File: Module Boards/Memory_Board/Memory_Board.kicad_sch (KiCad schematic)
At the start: 12 parts, among them U1 MX25U12832FZNI02-TR, U2 MX25U25643GZ4I00-T

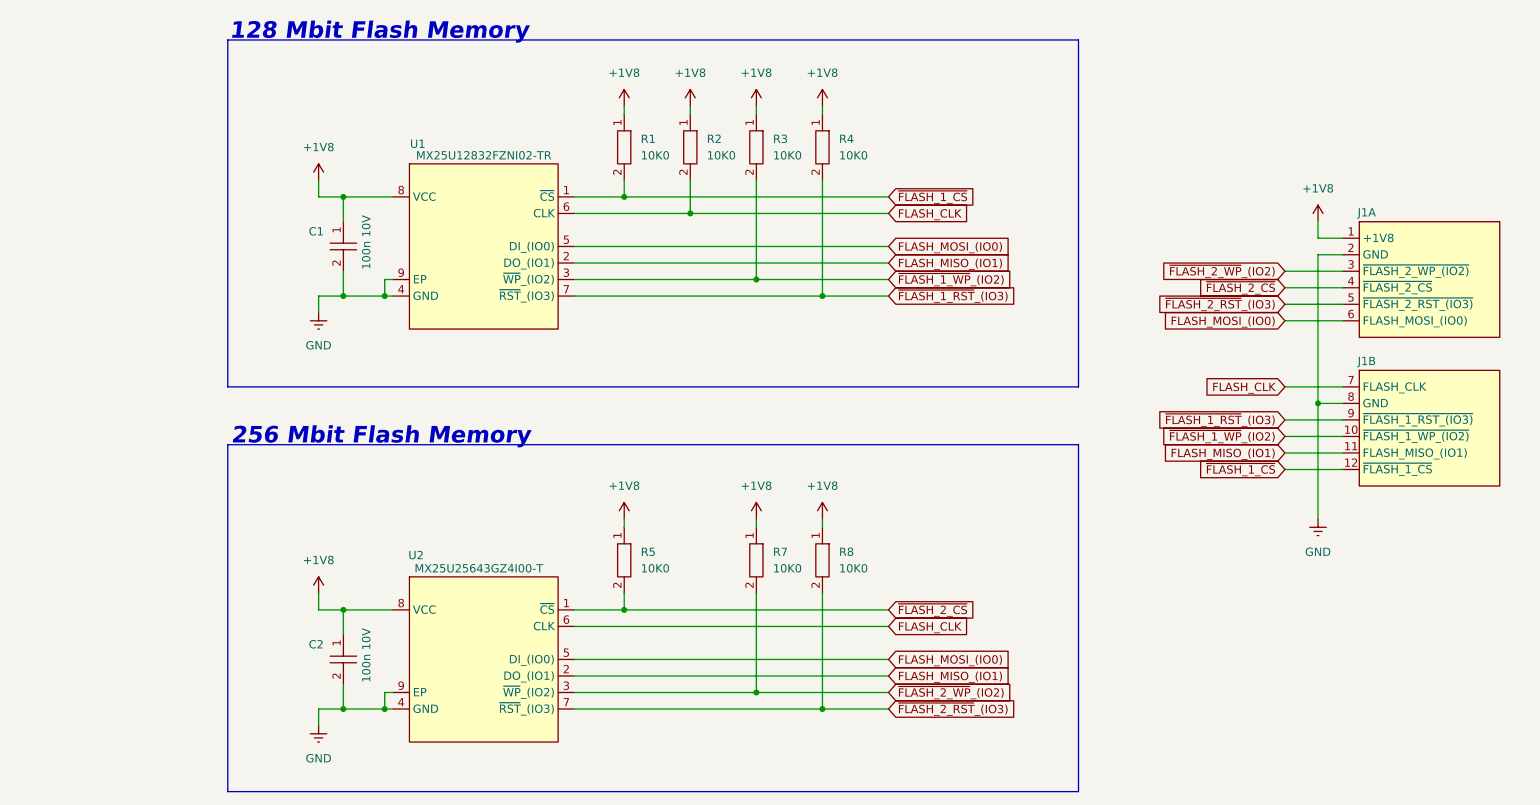
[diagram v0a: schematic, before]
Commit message: Added Memory Socket Board. Improved layout of the Module Board
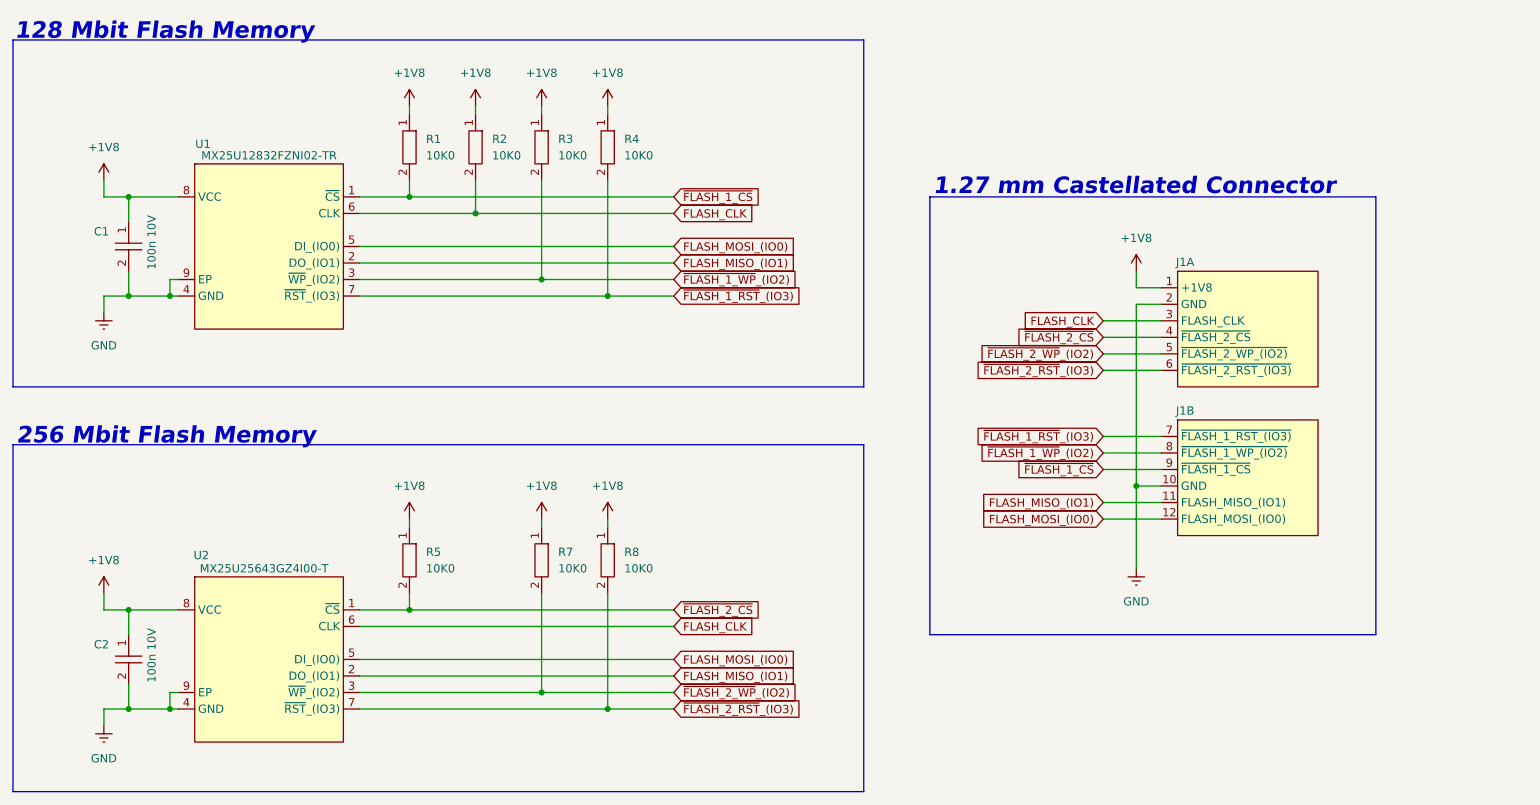
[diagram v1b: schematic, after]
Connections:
- net FLASH_CLK: now also J1.3 (FLASH_CLK); no longer J1.7 (FLASH_CLK)
- net FLASH_MOSI_(IO0): now also J1.12 (FLASH_MOSI_(IO0)); no longer J1.6 (FLASH_MOSI_(IO0))
- net GND: now also J1.10 (GND); no longer J1.8 (GND)
- net ~{FLASH_1_CS}: now also J1.9 (~{FLASH_1_CS}); no longer J1.12 (~{FLASH_1_CS})
- net ~{FLASH_1_RST}_(IO3): now also J1.7 (~{FLASH_1_RST_(IO3)}); no longer J1.9 (~{FLASH_1_RST_(IO3)})
- net ~{FLASH_1_WP}_(IO2): now also J1.8 (~{FLASH_1_WP_(IO2)}); no longer J1.10 (~{FLASH_1_WP_(IO2)})
- net ~{FLASH_2_RST}_(IO3): now also J1.6 (~{FLASH_2_RST_(IO3)}); no longer J1.5 (~{FLASH_2_RST_(IO3)})
- net ~{FLASH_2_WP}_(IO2): now also J1.5 (~{FLASH_2_WP_(IO2)}); no longer J1.3 (~{FLASH_2_WP_(IO2)})
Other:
- note added: "1.27 mm Castellated Connector"
- moved on the sheet: C1, C2, J1A, J1B, R1, R2, R3, R4, R5, R7, R8, U1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
